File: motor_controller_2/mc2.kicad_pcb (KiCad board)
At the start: 2 copper layers, 57 parts, among them P1 Battery, P2 Servo, P3 Uart, P4 Ultrasound, P5 Motor left, P6 Motor right, P7 ISP, P8 RPi 5V, U1 TS1117E33, U10 ts321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

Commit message: footprints finalized
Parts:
- D10: footprint Diodes_SMD:DO-214AB_Handsoldering -> Diodes_SMD:DO-214BA
- moved C10 70.4 mm to (111.8, 149.9)
- moved C14 70.4 mm to (102.9, 149.9)
- moved C21 70.4 mm to (120.7, 158.8)
- moved C81 70.4 mm to (120.7, 154.9)
- moved D10 70.4 mm to (88.9, 141.0)
- moved D11 70.4 mm to (113.0, 156.2)
- moved D60 70.4 mm to (106.7, 156.2)
- moved P1 70.4 mm to (119.4, 176.5)
- moved P2 70.4 mm to (100.3, 174.0)
- moved P5 70.4 mm to (87.6, 181.6)
- moved P7 70.4 mm to (106.7, 174.0)
- moved P8 70.4 mm to (73.7, 184.2)
- moved U10 70.4 mm to (101.6, 156.2)
- moved U4 70.4 mm to (47.0, 174.0)
- moved U6 70.4 mm to (86.4, 158.8)
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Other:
- board outline added: 120 x 55 mm

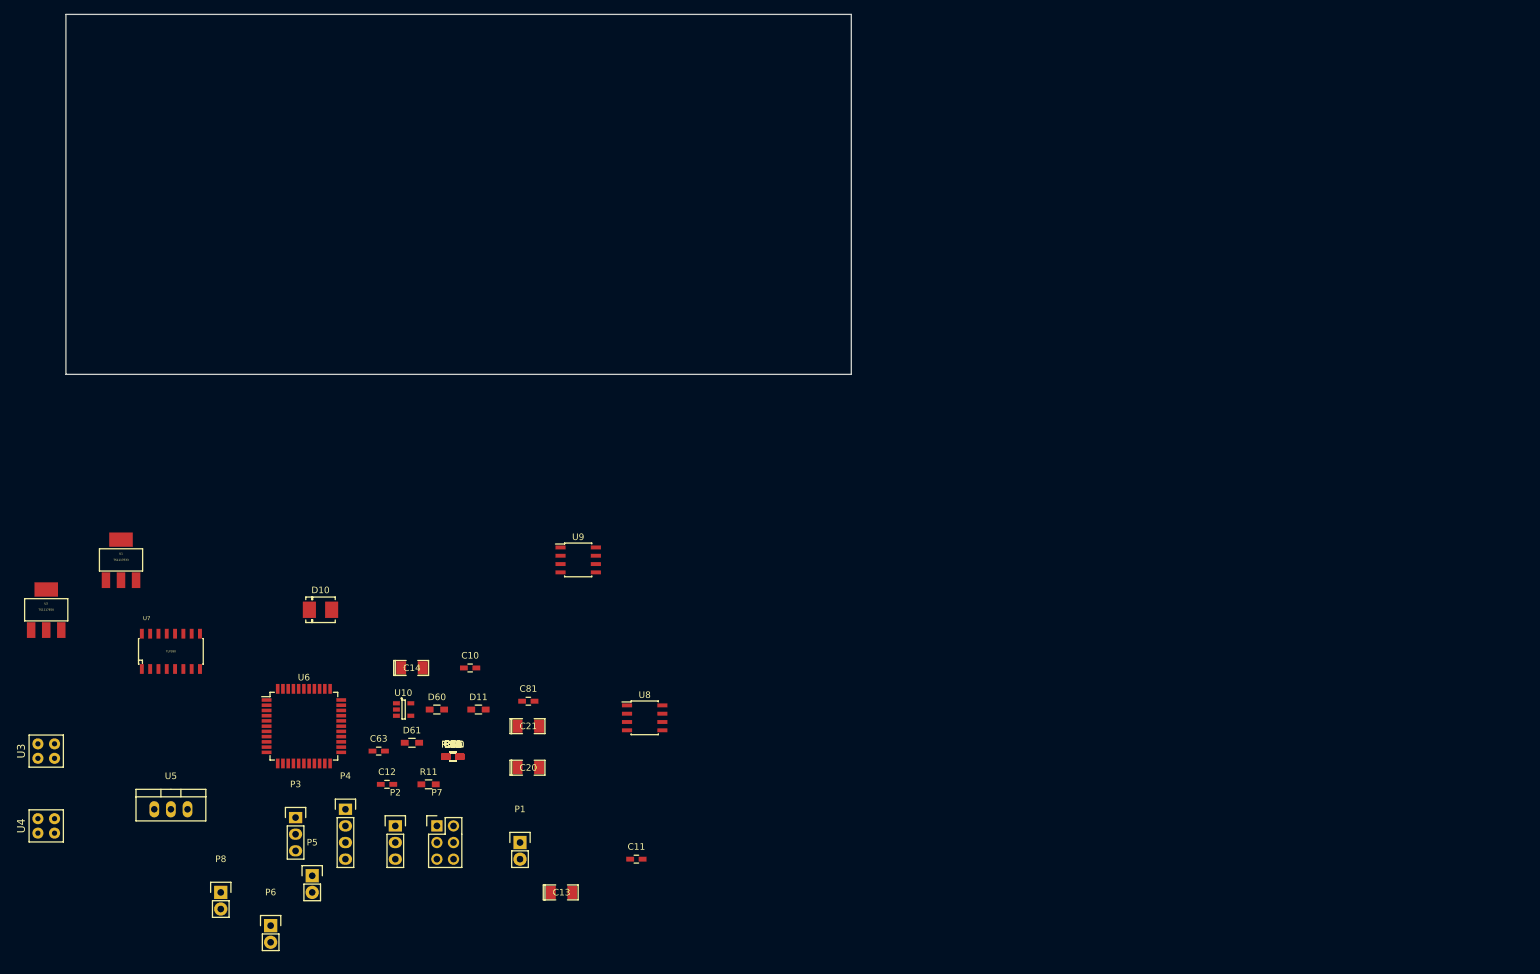
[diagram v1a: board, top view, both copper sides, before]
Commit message: component layout of motor controller
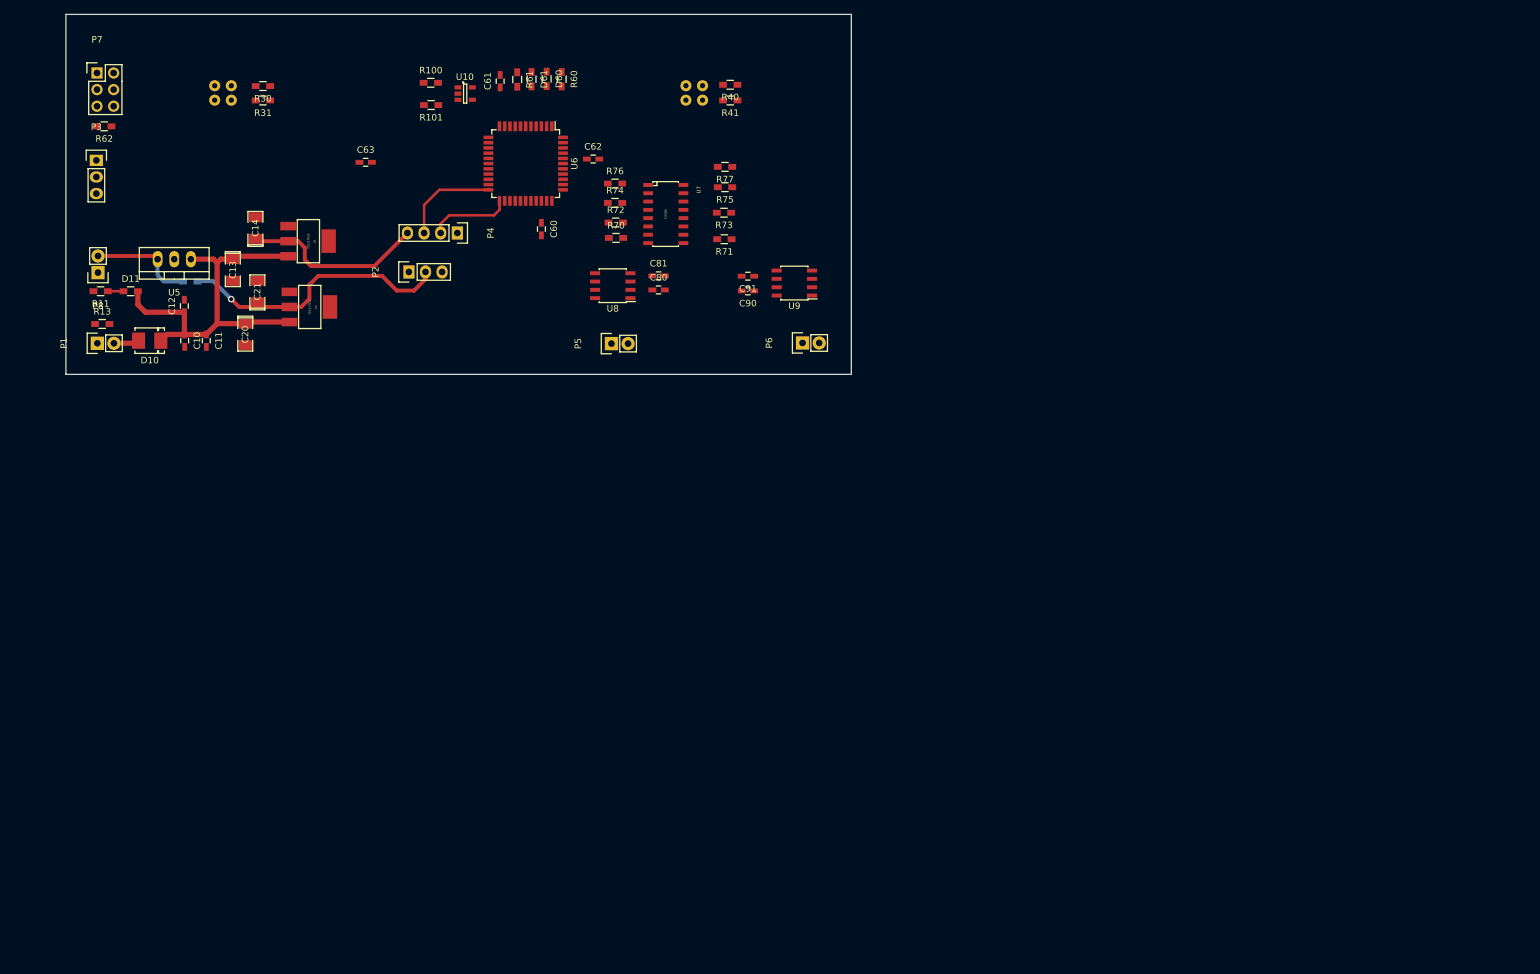
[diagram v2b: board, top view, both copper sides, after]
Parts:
- R12, U3, U4: moved to B.Cu
- moved U4 149.5 mm to (146.0, 62.0)
- moved P7 126.2 mm to (54.8, 59.0)
- moved P6 120.5 mm to (162.6, 100.2), turned to 90 degrees
- moved R40 111.1 mm to (151.5, 60.8), turned to 180 degrees
- moved R62 110.1 mm to (55.9, 67.1), turned to 180 degrees
- moved R41 108.9 mm to (151.5, 63.1), turned to 180 degrees
- moved C13 107.6 mm to (75.5, 89.0), turned to 270 degrees
- moved R30 106.5 mm to (80.1, 61.0), turned to 180 degrees
- moved P3 104.9 mm to (54.6, 72.3)
- moved R60 104.8 mm to (125.8, 59.9), turned to 270 degrees
- moved R31 104.4 mm to (80.1, 63.1), turned to 180 degrees
- moved U3 104.1 mm to (74.0, 62.0)
- moved R61 103.9 mm to (119.0, 60.0), turned to 270 degrees
- moved C61 103.5 mm to (116.3, 60.2), turned to 90 degrees
- moved R100 103.0 mm to (105.8, 60.5)
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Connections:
- P7 pad 3: Net-(P7-Pad3) -> (no net)
- P7 pad 4: Net-(P7-Pad4) -> (no net)
- R41 pad 2: /Rpm_left -> /Rpm_right
- U4 pad 4: /Rpm_left -> /Rpm_right
- U6 pad 1: Net-(U6-Pad1) -> (no net)
- U6 pad 11: Net-(U6-Pad11) -> (no net)
- U6 pad 14: Net-(U6-Pad14) -> (no net)
- U6 pad 15: Net-(U6-Pad15) -> (no net)
- U6 pad 16: Net-(U6-Pad16) -> (no net)
- U6 pad 17: Net-(U6-Pad17) -> (no net)
- U6 pad 2: Net-(U6-Pad2) -> (no net)
- U6 pad 24: Net-(U6-Pad24) -> (no net)
- U6 pad 25: Net-(U6-Pad25) -> (no net)
- U6 pad 26: Net-(U6-Pad26) -> (no net)
- U6 pad 27: Net-(U6-Pad27) -> (no net)
- U6 pad 36: Net-(U6-Pad36) -> (no net)
- U6 pad 37: Net-(U6-Pad37) -> (no net)
- U6 pad 40: Net-(U6-Pad40) -> (no net)
- U6 pad 41: Net-(U6-Pad41) -> (no net)
- U6 pad 42: Net-(U6-Pad42) -> (no net)
- U6 pad 43: Net-(U6-Pad43) -> (no net)
- U6 pad 44: Net-(U6-Pad44) -> (no net)
- U7 pad 1: Net-(R70-Pad2) -> Net-(R76-Pad2)
- U7 pad 10: /Reverse_right_i -> /Forward_left_i
- U7 pad 12: /Forward_right_i -> /Reverse_left_i
- U7 pad 14: /Reverse_left_i -> /Forward_right_i
- U7 pad 16: /Forward_left_i -> /Reverse_right_i
- U7 pad 3: Net-(R72-Pad2) -> Net-(R74-Pad2)
- U7 pad 5: Net-(R74-Pad2) -> Net-(R72-Pad2)
- U7 pad 7: Net-(R76-Pad2) -> Net-(R70-Pad2)
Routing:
- net +BATT: track 0.00 -> 59.3 mm
- net +5V: track 0.00 -> 42.4 mm, vias 0 -> 1
- net +3V3: track 0.00 -> 28.1 mm
- net +5VD: track 0.00 -> 16.1 mm
- net /Pulse_out: track 0.00 -> 15.1 mm
- net /Pulse_in: track 0.00 -> 12.6 mm
- net Net-(D10-Pad2): track 0.00 -> 3.93 mm
- net Net-(D11-Pad1): track 0.00 -> 2.40 mm
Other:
- net class Batt added: clearance 0.4, trace_width 0.8, via_dia 1, via_drill 0.6
- net class Default: trace_width 0.25 -> 0.4; via_dia 0.6 -> 1; via_drill 0.4 -> 0.6
- net class Vsupp added: clearance 0.2, trace_width 0.6, via_dia 1, via_drill 0.6

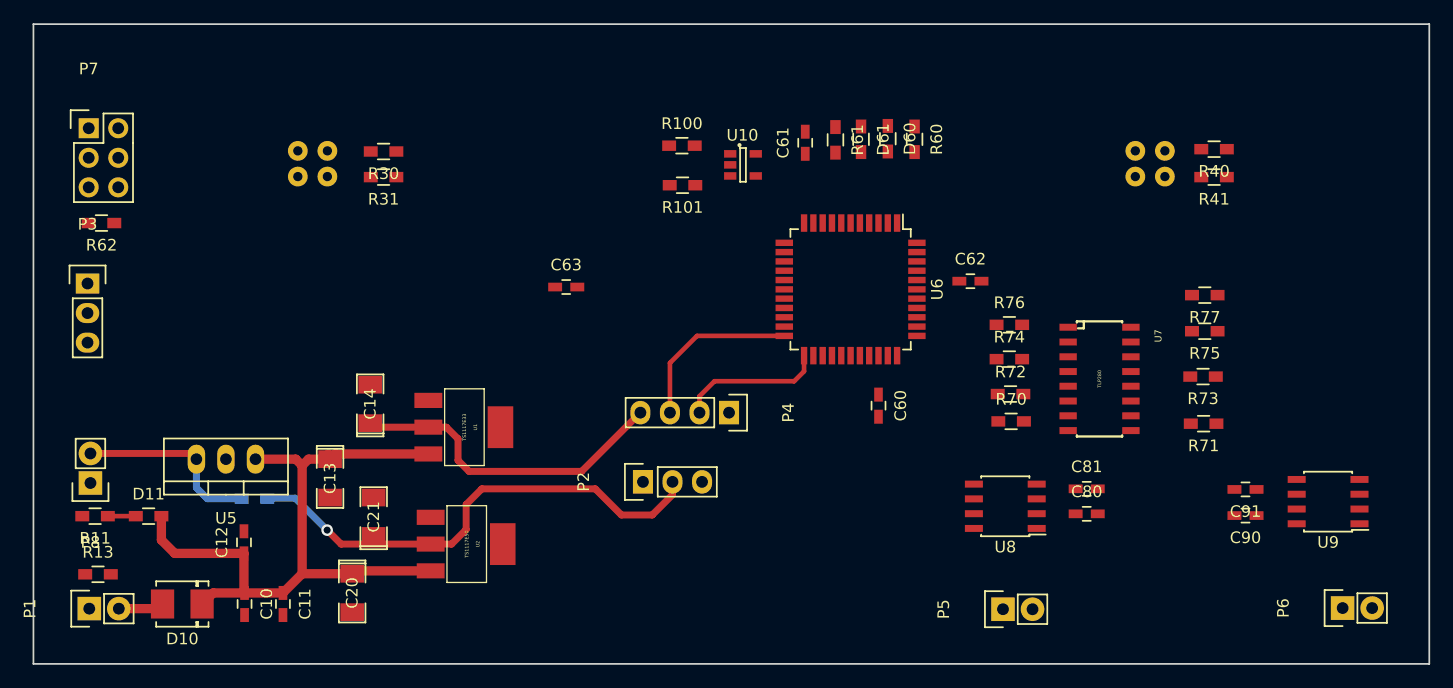
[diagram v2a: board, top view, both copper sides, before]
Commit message: pcb wiring (not ready)
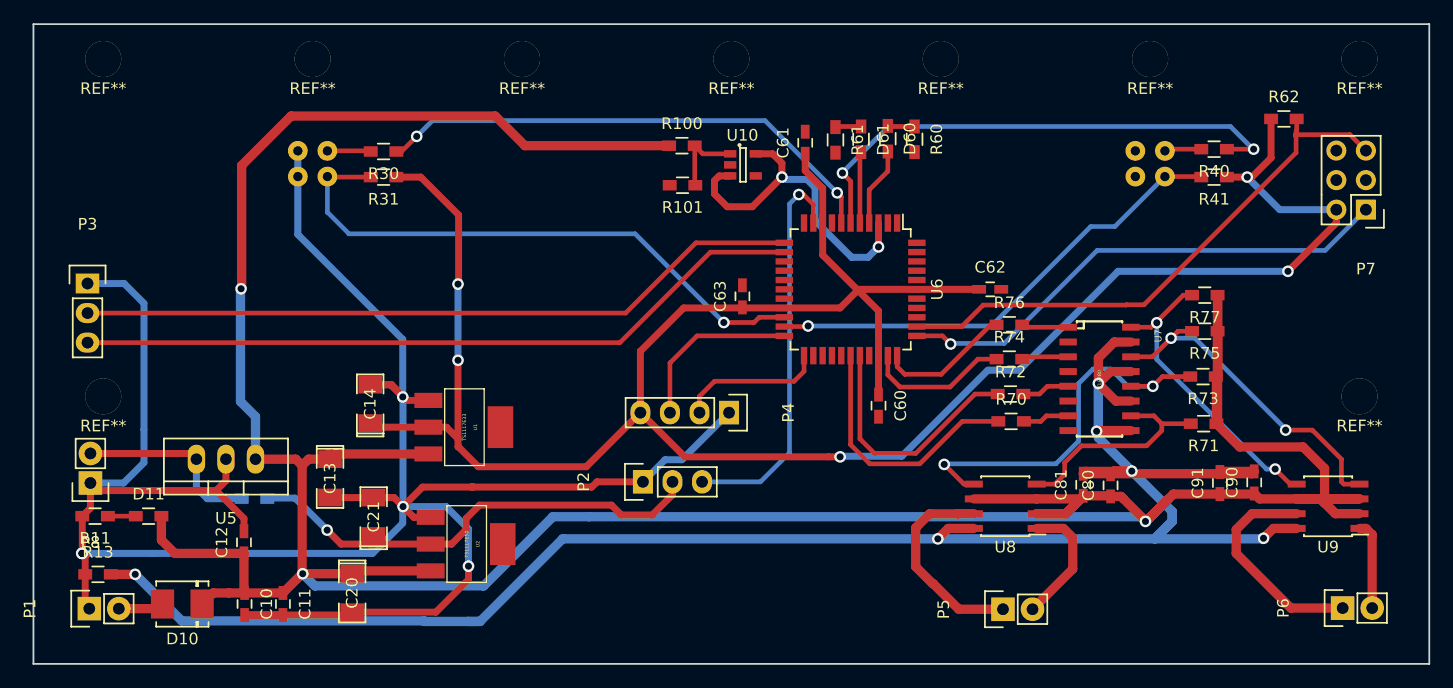
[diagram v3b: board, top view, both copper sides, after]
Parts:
- added REF**: 3mm hole, rzfp:3mm_hole, F.Cu at (164.0, 82.0)
- added REF**: 3mm hole, rzfp:3mm_hole, F.Cu at (56.0, 82.0)
- added REF**: 3mm hole, rzfp:3mm_hole, F.Cu at (56.0, 53.0)
- added REF**: 3mm hole, rzfp:3mm_hole, F.Cu at (74.0, 53.0)
- added REF**: 3mm hole, rzfp:3mm_hole, F.Cu at (92.0, 53.0)
- added REF**: 3mm hole, rzfp:3mm_hole, F.Cu at (110.0, 53.0)
- added REF**: 3mm hole, rzfp:3mm_hole, F.Cu at (128.0, 53.0)
- added REF**: 3mm hole, rzfp:3mm_hole, F.Cu at (146.0, 53.0)
- added REF**: 3mm hole, rzfp:3mm_hole, F.Cu at (164.0, 53.0)
- moved P7 110.0 mm to (164.6, 66.0), turned to 180 degrees
- moved R62 102.0 mm to (157.5, 58.1), turned to 0 degrees
- moved C63 15.2 mm to (111.0, 73.4), turned to 90 degrees
- moved C80 3.19 mm to (142.6, 89.7), turned to 90 degrees
- moved C90 2.95 mm to (154.9, 89.4), turned to 90 degrees
- moved C91 2.27 mm to (152.0, 89.5), turned to 90 degrees
- moved C62 1.84 mm to (132.2, 72.8)
- moved C81 0.46 mm to (140.2, 89.6), turned to 90 degrees
- moved U9 0.40 mm to (161.3, 91.5)
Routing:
- net +BATT: track 59.3 -> 298.5 mm, vias 0 -> 3
- net GND: track 0.00 -> 205.3 mm, vias 0 -> 5
- net +3V3: track 28.1 -> 200.5 mm, vias 0 -> 5
- net GNDPWR: track 0.00 -> 170.5 mm, vias 0 -> 6
- net /TX: track 0.00 -> 63.1 mm
- net /RX: track 0.00 -> 62.4 mm
- net /Rpm_left: track 0.00 -> 50.2 mm, vias 0 -> 1
- net /PDI_Clock: track 0.00 -> 49.0 mm
- net /IR_right: track 0.00 -> 44.8 mm, vias 0 -> 2
- net /IR_left: track 0.00 -> 44.3 mm, vias 0 -> 2
- net /PDI_Data: track 0.00 -> 43.7 mm, vias 0 -> 1
- net /Rpm_right: track 0.00 -> 41.1 mm, vias 0 -> 1
- net /Servo_pwm: track 0.00 -> 34.3 mm, vias 0 -> 1
- net /Reverse_left_i: track 0.00 -> 33.6 mm, vias 0 -> 2
- net /Forward_right_i: track 0.00 -> 29.1 mm, vias 0 -> 2
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
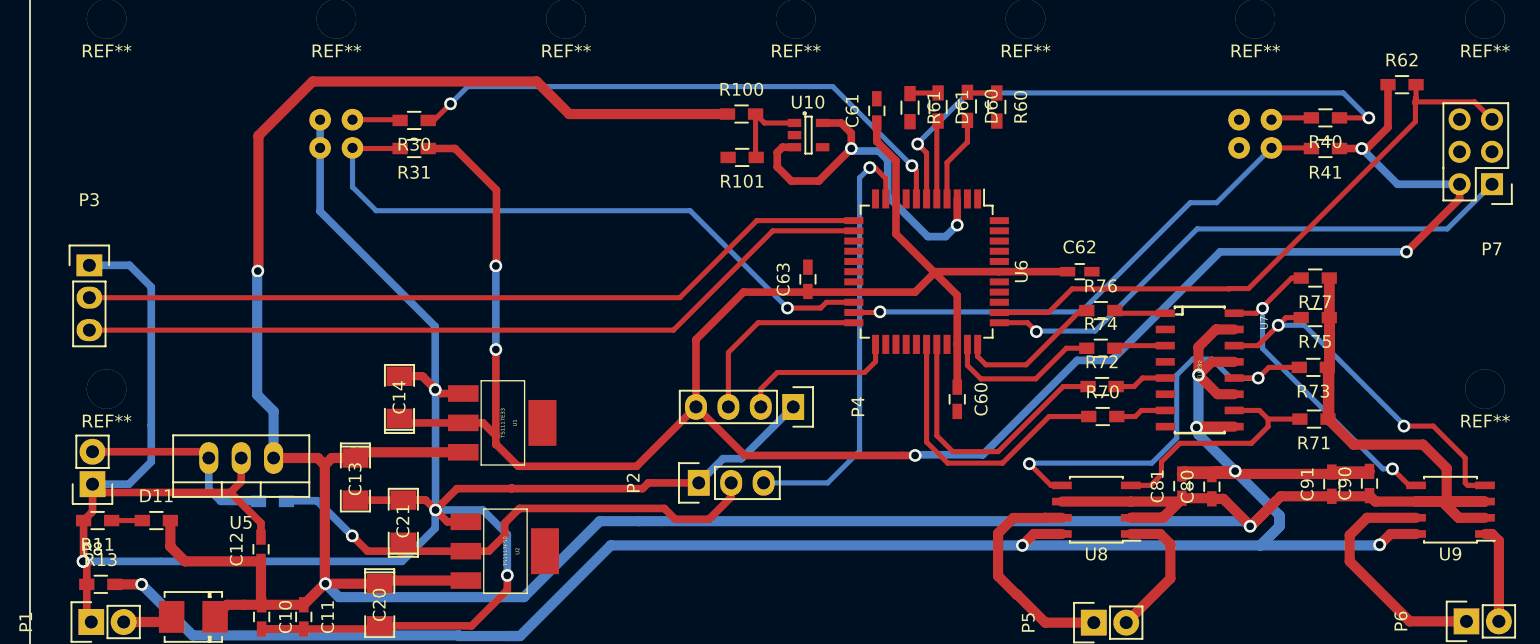
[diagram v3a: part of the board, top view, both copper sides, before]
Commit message: component pins checked
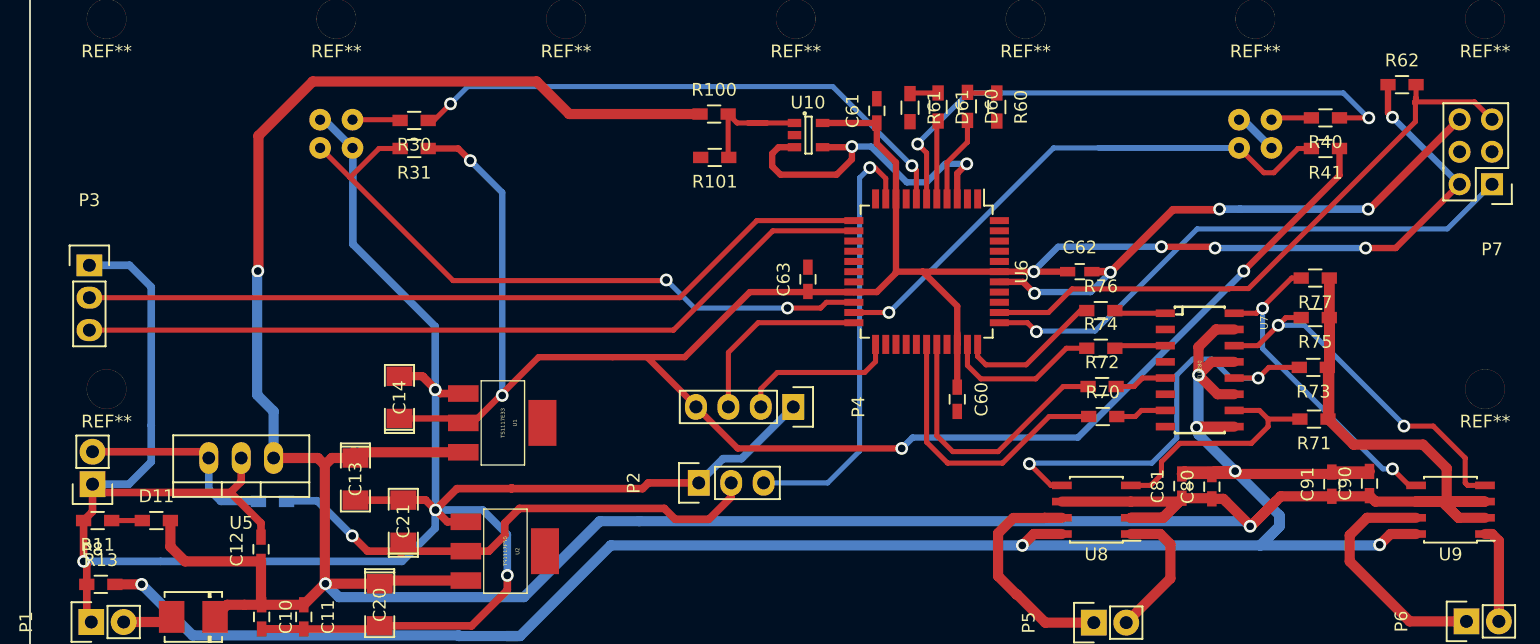
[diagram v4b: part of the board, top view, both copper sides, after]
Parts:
- moved R100 2.15 mm to (103.6, 60.5)
- moved R101 2.15 mm to (103.7, 63.9)
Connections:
- P7 pad 3: (no net) -> Net-(P7-Pad3)
- P7 pad 4: (no net) -> Net-(P7-Pad4)
- U10 pad 4: (no net) -> /ADC_Vbatt
- U10 pad 5: /ADC_Vbatt -> +3V3
- U6 pad 1: (no net) -> Net-(U6-Pad1)
- U6 pad 11: (no net) -> Net-(U6-Pad11)
- U6 pad 14: (no net) -> Net-(U6-Pad14)
- U6 pad 15: (no net) -> Net-(U6-Pad15)
- U6 pad 16: (no net) -> Net-(U6-Pad16)
- U6 pad 17: (no net) -> Net-(U6-Pad17)
- U6 pad 2: (no net) -> Net-(U6-Pad2)
- U6 pad 24: (no net) -> Net-(U6-Pad24)
- U6 pad 25: (no net) -> Net-(U6-Pad25)
- U6 pad 26: (no net) -> Net-(U6-Pad26)
- U6 pad 27: (no net) -> Net-(U6-Pad27)
- U6 pad 36: (no net) -> Net-(U6-Pad36)
- U6 pad 37: (no net) -> Net-(U6-Pad37)
- U6 pad 40: (no net) -> Net-(U6-Pad40)
- U6 pad 41: (no net) -> Net-(U6-Pad41)
- U6 pad 42: (no net) -> Net-(U6-Pad42)
- U6 pad 43: (no net) -> Net-(U6-Pad43)
- U6 pad 44: (no net) -> Net-(U6-Pad44)
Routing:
- net GND: track 205.3 -> 252.6 mm, vias 5 -> 8
- net +3V3: track 200.5 -> 223.2 mm, vias 5 -> 9
- net /Rpm_right: track 41.1 -> 53.8 mm
- net Net-(R100-Pad2): track 6.76 -> 10.4 mm
- net +BATT: track 298.5 -> 296.3 mm
- net /Rpm_left: track 50.2 -> 52.1 mm, vias 1 -> 2
- net /ADC_Vbatt: track 29.0 -> 27.1 mm
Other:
- net class Vsupp: trace_width 0.6 -> 0.5

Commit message: pcb wiring done
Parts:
- R12: moved to F.Cu
- moved P2 31.3 mm to (107.8, 58.5)
- moved C80 17.8 mm to (125.0, 92.5), turned to 180 degrees
- moved U10 12.4 mm to (98.6, 63.1)
- moved R31 12.4 mm to (67.8, 63.0), turned to 0 degrees
- moved R100 12.1 mm to (92.0, 64.0)
- moved R101 12.1 mm to (92.0, 60.8)
- moved C81 12.1 mm to (128.2, 88.5)
- moved C14 11.7 mm to (78.8, 71.0)
- moved R41 11.0 mm to (140.5, 63.0), turned to 0 degrees
- moved R60 10.3 mm to (136.0, 60.5)
- moved D60 10.1 mm to (133.5, 60.5)
- moved D61 9.87 mm to (131.0, 60.5)
- moved R61 9.57 mm to (128.5, 60.5)
- moved U1 9.18 mm to (87.8, 75.5)
- moved P3 8.05 mm to (54.5, 64.2)
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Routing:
- net GND: track 252.6 -> 411.4 mm, vias 8 -> 12
- net +BATT: track 296.3 -> 251.7 mm, vias 3 -> 5
- net +5V: track 41.6 -> 85.8 mm, vias 1 -> 4
- net +3V3: track 223.2 -> 196.8 mm, vias 9 -> 6
- net /Servo_pwm: track 34.3 -> 9.72 mm, vias 1 -> 0
- net /LED0: track 6.81 -> 20.3 mm
- net /LED1: track 6.14 -> 18.5 mm
- net /Rpm_right: track 53.8 -> 41.8 mm, vias 1 -> 2
- net /PDI_Data: track 43.7 -> 53.8 mm
- net /Reverse_right: track 11.5 -> 19.4 mm
- net /Motor_right_out2: track 18.9 -> 11.3 mm
- net /Forward_right: track 12.4 -> 19.5 mm
- net /Reverse_left: track 21.6 -> 28.5 mm
- net /PDI_Clock: track 49.0 -> 55.8 mm, vias 0 -> 2
- net /Reverse_right_i: track 26.4 -> 32.9 mm, vias 2 -> 0
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- added copper zone on B.Cu, net GND
- added copper zone on F.Cu, net GND
- added copper zone on B.Cu, net GNDPWR
- added copper zone on F.Cu, net GNDPWR
